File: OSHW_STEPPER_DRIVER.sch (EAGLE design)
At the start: 60 parts, among them X2 MSTBA2, X3 MSTBA4

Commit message: modified:   OSHW_STEPPER_DRIVER.sch
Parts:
- added J1: (no value), STAR_POINTS:STARBOARD_GND
- added LED1: (no value), led:LEDSIDELED
- added R27: 180, rcl:R-EU_R0603
- R2: device resistor:R-TRIMM3296Y -> resistor:R-TRIMM3296P
- R3, R4: device rcl:R-EU_R0805 -> rcl:R-EU_R0603
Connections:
- new net N$17: LED1.A, R27.1
- new net N$4: J1.P$1, X2-1.1
- new net PGND: C1.2, C14.-, C15.2, C16.-, C17.2, C6.-, C7.-, J1.P$2, R20.1, R21.1, R22.1, R23.1
- net GND: now also J1.MOUNT, LED1.C; no longer C1.2, C14.-, C15.2, C16.-, C17.2, C6.-, C7.-, R20.1, R21.1, R22.1, R23.1, X2-1.1
- net VDD: now also R27.2

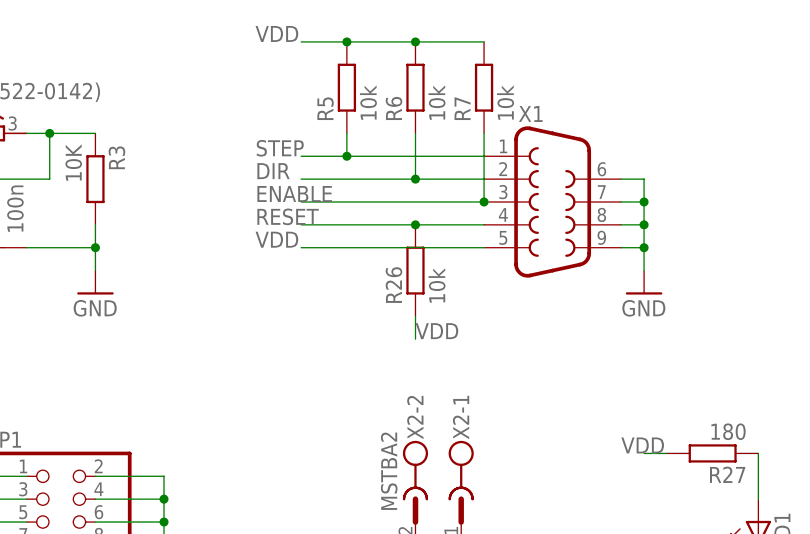
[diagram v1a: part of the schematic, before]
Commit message: minor fix, added teardrops
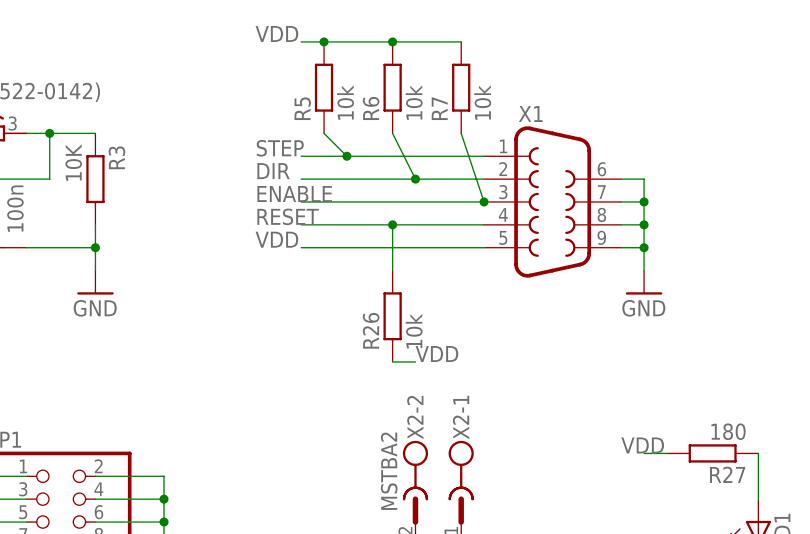
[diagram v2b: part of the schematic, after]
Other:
- moved on the sheet: R26, R5, R6, R7
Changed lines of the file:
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@@
 <?xml version="1.0" encoding="utf-8"?>
 <!DOCTYPE eagle SYSTEM "eagle.dtd">
-<eagle version="6.4">
+<eagle version="6.2">
 <drawing>
 <settings>
@@
 <instance part="X1" gate="G$1" x="-45.72" y="45.72"/>
 <instance part="GND5" gate="1" x="-35.56" y="35.56"/>
-<instance part="R5" gate="G$1" x="-68.58" y="58.42" rot="R90"/>
-<instance part="R6" gate="G$1" x="-60.96" y="58.42" rot="R90"/>
-<instance part="R7" gate="G$1" x="-53.34" y="58.42" rot="R90"/>
+<instance part="R5" gate="G$1" x="-71.12" y="58.42" rot="R90"/>
+<instance part="R6" gate="G$1" x="-63.5" y="58.42" rot="R90"/>
+<instance part="R7" gate="G$1" x="-55.88" y="58.42" rot="R90"/>
 <instance part="JP1" gate="A" x="-101.6" y="10.16"/>
 <instance part="GND6" gate="1" x="-88.9" y="-2.54"/>
@@
 <instance part="C12" gate="G$1" x="-101.6" y="-25.4"/>
 <instance part="C13" gate="G$1" x="-86.36" y="-25.4"/>
-<instance part="R26" gate="G$1" x="-60.96" y="38.1" rot="R90"/>
+<instance part="R26" gate="G$1" x="-63.5" y="33.02" rot="R90"/>
 <instance part="C14" gate="G$1" x="-60.96" y="-25.4"/>
 <instance part="C15" gate="G$1" x="-53.34" y="-20.32"/>
@@
 <pinref part="R7" gate="G$1" pin="2"/>
 <pinref part="R6" gate="G$1" pin="2"/>
-<wire x1="-53.34" y1="63.5" x2="-60.96" y2="63.5" width="0.1524" layer="91"/>
+<wire x1="-55.88" y1="63.5" x2="-63.5" y2="63.5" width="0.1524" layer="91"/>
 <pinref part="R5" gate="G$1" pin="2"/>
-<wire x1="-60.96" y1="63.5" x2="-68.58" y2="63.5" width="0.1524" layer="91"/>
-<junction x="-60.96" y="63.5"/>
-<wire x1="-68.58" y1="63.5" x2="-73.66" y2="63.5" width="0.1524" layer="91"/>
-<junction x="-68.58" y="63.5"/>
+<wire x1="-63.5" y1="63.5" x2="-71.12" y2="63.5" width="0.1524" layer="91"/>
+<junction x="-63.5" y="63.5"/>
+<wire x1="-71.12" y1="63.5" x2="-73.66" y2="63.5" width="0.1524" layer="91"/>
+<junction x="-71.12" y="63.5"/>
 <label x="-78.74" y="63.5" size="1.778" layer="95"/>
 </segment>
@@
 <segment>
 <pinref part="R26" gate="G$1" pin="1"/>
-<wire x1="-60.96" y1="33.02" x2="-60.96" y2="30.48" width="0.1524" layer="91"/>
-<label x="-60.96" y="30.48" size="1.778" layer="95"/>
+<wire x1="-63.5" y1="27.94" x2="-60.96" y2="27.94" width="0.1524" layer="91"/>
+<label x="-60.96" y="27.94" size="1.778" layer="95"/>
 </segment>
 <segment>
@@
 <pinref part="R6" gate="G$1" pin="1"/>
 <wire x1="-60.96" y1="48.26" x2="-73.66" y2="48.26" width="0.1524" layer="91"/>
-<wire x1="-60.96" y1="53.34" x2="-60.96" y2="48.26" width="0.1524" layer="91"/>
+<wire x1="-63.5" y1="53.34" x2="-60.96" y2="48.26" width="0.1524" layer="91"/>
 <junction x="-60.96" y="48.26"/>
 </segment>
@@
 <label x="-78.74" y="45.72" size="1.778" layer="95"/>
 <pinref part="R7" gate="G$1" pin="1"/>
-<wire x1="-53.34" y1="53.34" x2="-53.34" y2="45.72" width="0.1524" layer="91"/>
+<wire x1="-55.88" y1="53.34" x2="-53.34" y2="45.72" width="0.1524" layer="91"/>
 <junction x="-53.34" y="45.72"/>
 </segment>
@@
 <pinref part="R5" gate="G$1" pin="1"/>
 <wire x1="-68.58" y1="50.8" x2="-73.66" y2="50.8" width="0.1524" layer="91"/>
-<wire x1="-68.58" y1="53.34" x2="-68.58" y2="50.8" width="0.1524" layer="91"/>
+<wire x1="-71.12" y1="53.34" x2="-68.58" y2="50.8" width="0.1524" layer="91"/>
 <junction x="-68.58" y="50.8"/>
 </segment>
@@
 </segment>
 <segment>
+<label x="-78.74" y="43.18" size="1.778" layer="95"/>
 <pinref part="X1" gate="G$1" pin="4"/>
-<wire x1="-53.34" y1="43.18" x2="-60.96" y2="43.18" width="0.1524" layer="91"/>
-<label x="-78.74" y="43.18" size="1.778" layer="95"/>
+<wire x1="-53.34" y1="43.18" x2="-63.5" y2="43.18" width="0.1524" layer="91"/>
 <pinref part="R26" gate="G$1" pin="2"/>
-<wire x1="-60.96" y1="43.18" x2="-73.66" y2="43.18" width="0.1524" layer="91"/>
-<junction x="-60.96" y="43.18"/>
+<wire x1="-63.5" y1="43.18" x2="-73.66" y2="43.18" width="0.1524" layer="91"/>
+<wire x1="-63.5" y1="38.1" x2="-63.5" y2="43.18" width="0.1524" layer="91"/>
+<junction x="-63.5" y="43.18"/>
 </segment>
 </net>
@@
 </sheet>
 </sheets>
-<errors>
-</errors>
 </schematic>
 </drawing>

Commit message: REF fix
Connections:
- net REF: now also C5.1
- net VDD: no longer C5.1
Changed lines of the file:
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@@
 <pinref part="R4" gate="G$1" pin="2"/>
 <wire x1="-119.38" y1="43.18" x2="-119.38" y2="40.64" width="0.1524" layer="91"/>
-<label x="-119.38" y="38.1" size="1.778" layer="95"/>
-<pinref part="C5" gate="G$1" pin="1"/>
-<wire x1="-111.76" y1="40.64" x2="-119.38" y2="40.64" width="0.1524" layer="91"/>
+<label x="-124.46" y="40.64" size="1.778" layer="95"/>
 </segment>
 <segment>
@@
 <pinref part="R2" gate="G$1" pin="E"/>
 <pinref part="R4" gate="G$1" pin="1"/>
-<wire x1="-119.38" y1="53.34" x2="-114.3" y2="53.34" width="0.1524" layer="91"/>
+<wire x1="-119.38" y1="53.34" x2="-116.84" y2="53.34" width="0.1524" layer="91"/>
 <junction x="-119.38" y="53.34"/>
 <label x="-129.54" y="53.34" size="1.778" layer="95"/>
+<pinref part="C5" gate="G$1" pin="1"/>
+<wire x1="-116.84" y1="53.34" x2="-114.3" y2="53.34" width="0.1524" layer="91"/>
+<wire x1="-111.76" y1="40.64" x2="-116.84" y2="40.64" width="0.1524" layer="91"/>
+<wire x1="-116.84" y1="40.64" x2="-116.84" y2="53.34" width="0.1524" layer="91"/>
+<junction x="-116.84" y="53.34"/>
 </segment>
 </net>

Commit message: updated Creg footprint and value
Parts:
- C4: value 100u -> 1u; device rcl:CPOL-US153CLV-0605 -> rcl:CPOL-US153CLV-0405
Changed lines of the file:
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@@
 <grid distance="0.1" unitdist="inch" unit="inch" style="lines" multiple="1" display="no" altdistance="0.01" altunitdist="inch" altunit="inch"/>
 <layers>
-<layer number="1" name="Top" color="4" fill="1" visible="no" active="no"/>
-<layer number="2" name="Route2" color="1" fill="3" visible="no" active="no"/>
-<layer number="3" name="Route3" color="4" fill="3" visible="no" active="no"/>
-<layer number="4" name="Route4" color="1" fill="4" visible="no" active="no"/>
-<layer number="5" name="Route5" color="4" fill="4" visible="no" active="no"/>
-<layer number="6" name="Route6" color="1" fill="8" visible="no" active="no"/>
-<layer number="7" name="Route7" color="4" fill="8" visible="no" active="no"/>
-<layer number="8" name="Route8" color="1" fill="2" visible="no" active="no"/>
-<layer number="9" name="Route9" color="4" fill="2" visible="no" active="no"/>
-<layer number="10" name="Route10" color="1" fill="7" visible="no" active="no"/>
-<layer number="11" name="Route11" color="4" fill="7" visible="no" active="no"/>
-<layer number="12" name="Route12" color="1" fill="5" visible="no" active="no"/>
-<layer number="13" name="Route13" color="4" fill="5" visible="no" active="no"/>
-<layer number="14" name="Route14" color="1" fill="6" visible="no" active="no"/>
-<layer number="15" name="Route15" color="4" fill="6" visible="no" active="no"/>
-<layer number="16" name="Bottom" color="1" fill="1" visible="no" active="no"/>
-<layer number="17" name="Pads" color="2" fill="1" visible="no" active="no"/>
-<layer number="18" name="Vias" color="2" fill="1" visible="no" active="no"/>
-<layer number="19" name="Unrouted" color="6" fill="1" visible="no" active="no"/>
-<layer number="20" name="Dimension" color="15" fill="1" visible="no" active="no"/>
-<layer number="21" name="tPlace" color="7" fill="1" visible="no" active="no"/>
-<layer number="22" name="bPlace" color="7" fill="1" visible="no" active="no"/>
-<layer number="23" name="tOrigins" color="15" fill="1" visible="no" active="no"/>
-<layer number="24" name="bOrigins" color="15" fill="1" visible="no" active="no"/>
-<layer number="25" name="tNames" color="7" fill="1" visible="no" active="no"/>
-<layer number="26" name="bNames" color="7" fill="1" visible="no" active="no"/>
-<layer number="27" name="tValues" color="7" fill="1" visible="no" active="no"/>
-<layer number="28" name="bValues" color="7" fill="1" visible="no" active="no"/>
+<layer number="1" name="Top" color="4" fill="1" visible="yes" active="no"/>
+<layer number="2" name="Route2" color="1" fill="3" visible="yes" active="no"/>
+<layer number="3" name="Route3" color="4" fill="3" visible="yes" active="no"/>
+<layer number="4" name="Route4" color="1" fill="4" visible="yes" active="no"/>
+<layer number="5" name="Route5" color="4" fill="4" visible="yes" active="no"/>
+<layer number="6" name="Route6" color="1" fill="8" visible="yes" active="no"/>
+<layer number="7" name="Route7" color="4" fill="8" visible="yes" active="no"/>
+<layer number="8" name="Route8" color="1" fill="2" visible="yes" active="no"/>
+<layer number="9" name="Route9" color="4" fill="2" visible="yes" active="no"/>
+<layer number="10" name="Route10" color="1" fill="7" visible="yes" active="no"/>
+<layer number="11" name="Route11" color="4" fill="7" visible="yes" active="no"/>
+<layer number="12" name="Route12" color="1" fill="5" visible="yes" active="no"/>
+<layer number="13" name="Route13" color="4" fill="5" visible="yes" active="no"/>
+<layer number="14" name="Route14" color="1" fill="6" visible="yes" active="no"/>
+<layer number="15" name="Route15" color="4" fill="6" visible="yes" active="no"/>
+<layer number="16" name="Bottom" color="1" fill="1" visible="yes" active="no"/>
+<layer number="17" name="Pads" color="2" fill="1" visible="yes" active="no"/>
+<layer number="18" name="Vias" color="2" fill="1" visible="yes" active="no"/>
+<layer number="19" name="Unrouted" color="6" fill="1" visible="yes" active="no"/>
+<layer number="20" name="Dimension" color="15" fill="1" visible="yes" active="no"/>
+<layer number="21" name="tPlace" color="7" fill="1" visible="yes" active="no"/>
+<layer number="22" name="bPlace" color="7" fill="1" visible="yes" active="no"/>
+<layer number="23" name="tOrigins" color="15" fill="1" visible="yes" active="no"/>
+<layer number="24" name="bOrigins" color="15" fill="1" visible="yes" active="no"/>
+<layer number="25" name="tNames" color="7" fill="1" visible="yes" active="no"/>
+<layer number="26" name="bNames" color="7" fill="1" visible="yes" active="no"/>
+<layer number="27" name="tValues" color="7" fill="1" visible="yes" active="no"/>
+<layer number="28" name="bValues" color="7" fill="1" visible="yes" active="no"/>
 <layer number="29" name="tStop" color="7" fill="3" visible="no" active="no"/>
 <layer number="30" name="bStop" color="7" fill="6" visible="no" active="no"/>
@@
 <layer number="35" name="tGlue" color="7" fill="4" visible="no" active="no"/>
 <layer number="36" name="bGlue" color="7" fill="5" visible="no" active="no"/>
-<layer number="37" name="tTest" color="7" fill="1" visible="no" active="no"/>
-<layer number="38" name="bTest" color="7" fill="1" visible="no" active="no"/>
+<layer number="37" name="tTest" color="7" fill="1" visible="yes" active="no"/>
+<layer number="38" name="bTest" color="7" fill="1" visible="yes" active="no"/>
 <layer number="39" name="tKeepout" color="4" fill="11" visible="no" active="no"/>
 <layer number="40" name="bKeepout" color="1" fill="11" visible="no" active="no"/>
@@
 <layer number="44" name="Drills" color="7" fill="1" visible="no" active="no"/>
 <layer number="45" name="Holes" color="7" fill="1" visible="no" active="no"/>
-<layer number="46" name="Milling" color="3" fill="1" visible="no" active="no"/>
-<layer number="47" name="Measures" color="7" fill="1" visible="no" active="no"/>
-<layer number="48" name="Document" color="7" fill="1" visible="no" active="no"/>
-<layer number="49" name="Reference" color="7" fill="1" visible="no" active="no"/>
-<layer number="50" name="dxf" color="7" fill="1" visible="no" active="no"/>
-<layer number="51" name="tDocu" color="7" fill="1" visible="no" active="no"/>
-<layer number="52" name="bDocu" color="7" fill="1" visible="no" active="no"/>
-<layer number="53" name="tGND_GNDA" color="7" fill="9" visible="no" active="no"/>
-<layer number="54" name="bGND_GNDA" color="1" fill="9" visible="no" active="no"/>
-<layer number="56" name="wert" color="7" fill="1" visible="no" active="no"/>
+<layer number="46" name="Milling" color="3" fill="1" visible="yes" active="no"/>
+<layer number="47" name="Measures" color="7" fill="1" visible="yes" active="no"/>
+<layer number="48" name="Document" color="7" fill="1" visible="yes" active="no"/>
+<layer number="49" name="Reference" color="7" fill="1" visible="yes" active="no"/>
+<layer number="50" name="dxf" color="7" fill="1" visible="yes" active="no"/>
+<layer number="51" name="tDocu" color="7" fill="1" visible="yes" active="no"/>
+<layer number="52" name="bDocu" color="7" fill="1" visible="yes" active="no"/>
+<layer number="53" name="tGND_GNDA" color="7" fill="9" visible="yes" active="no"/>
+<layer number="54" name="bGND_GNDA" color="1" fill="9" visible="yes" active="no"/>
+<layer number="56" name="wert" color="7" fill="1" visible="yes" active="no"/>
 <layer number="91" name="Nets" color="2" fill="1" visible="yes" active="yes"/>
 <layer number="92" name="Busses" color="1" fill="1" visible="yes" active="yes"/>
@@
 <part name="GND1" library="supply1" deviceset="GND" device="" value="GND"/>
 <part name="C3" library="rcl" deviceset="CPOL-US" device="153CLV-0605" value="100u"/>
-<part name="C4" library="rcl" deviceset="CPOL-US" device="153CLV-0605" value="100u"/>
+<part name="C4" library="rcl" deviceset="CPOL-US" device="153CLV-0405" value="1u"/>
 <part name="GND2" library="supply1" deviceset="GND" device="" value="GND"/>
 <part name="R1" library="rcl" deviceset="R-EU_" device="R0805" value="10K 10ppm (662-1252)"/>
